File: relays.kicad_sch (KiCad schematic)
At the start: 0 parts

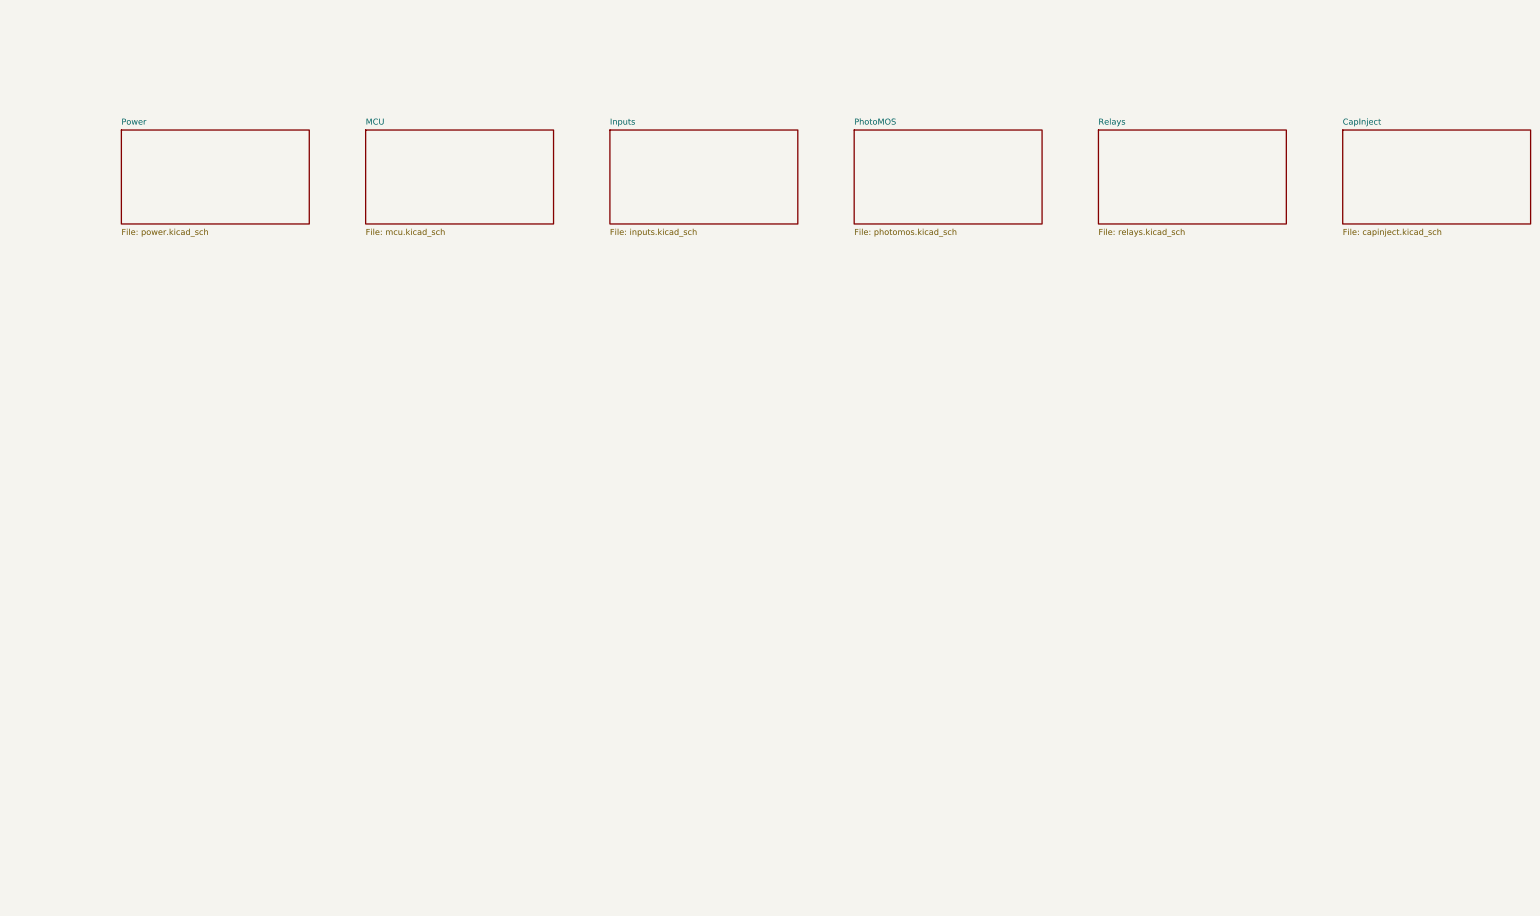
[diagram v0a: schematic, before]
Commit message: Realize ERC-clean KiCad schematic (rev 0.2)
Turn the paper design into a real KiCad 10 hierarchical schematic with
library symbols and footprints. 6 sheets: power, MCU, and full channel
counts (8 inputs, 8 PhotoMOS, 2 relays, 4 cap-inject) = 160 components.

- Replace AMS1117 with SY8089 buck (2.7-5.5Vin) for Wi-Fi-peak headroom.
- Input front-end uses 2.2k/1206 + EL357N (CRD dropped; poor LCSC stock).
- Verify key parts against JLCPCB (ESP32-S3 C2913198, SY8089 C78988,
  AQY212GS C719745, HK4100F C12072, USB-C C165948, AO3400A C20917).
- ERC passes 0 errors / 0 warnings; netlist verified, isolation barrier
  confirmed intact. No PCB layout yet (per request).
- Add Python generator (gen/) that emits the project and custom symbols.

Co-Authored-By: Claude Opus 4.7 <noreply@anthropic.com>
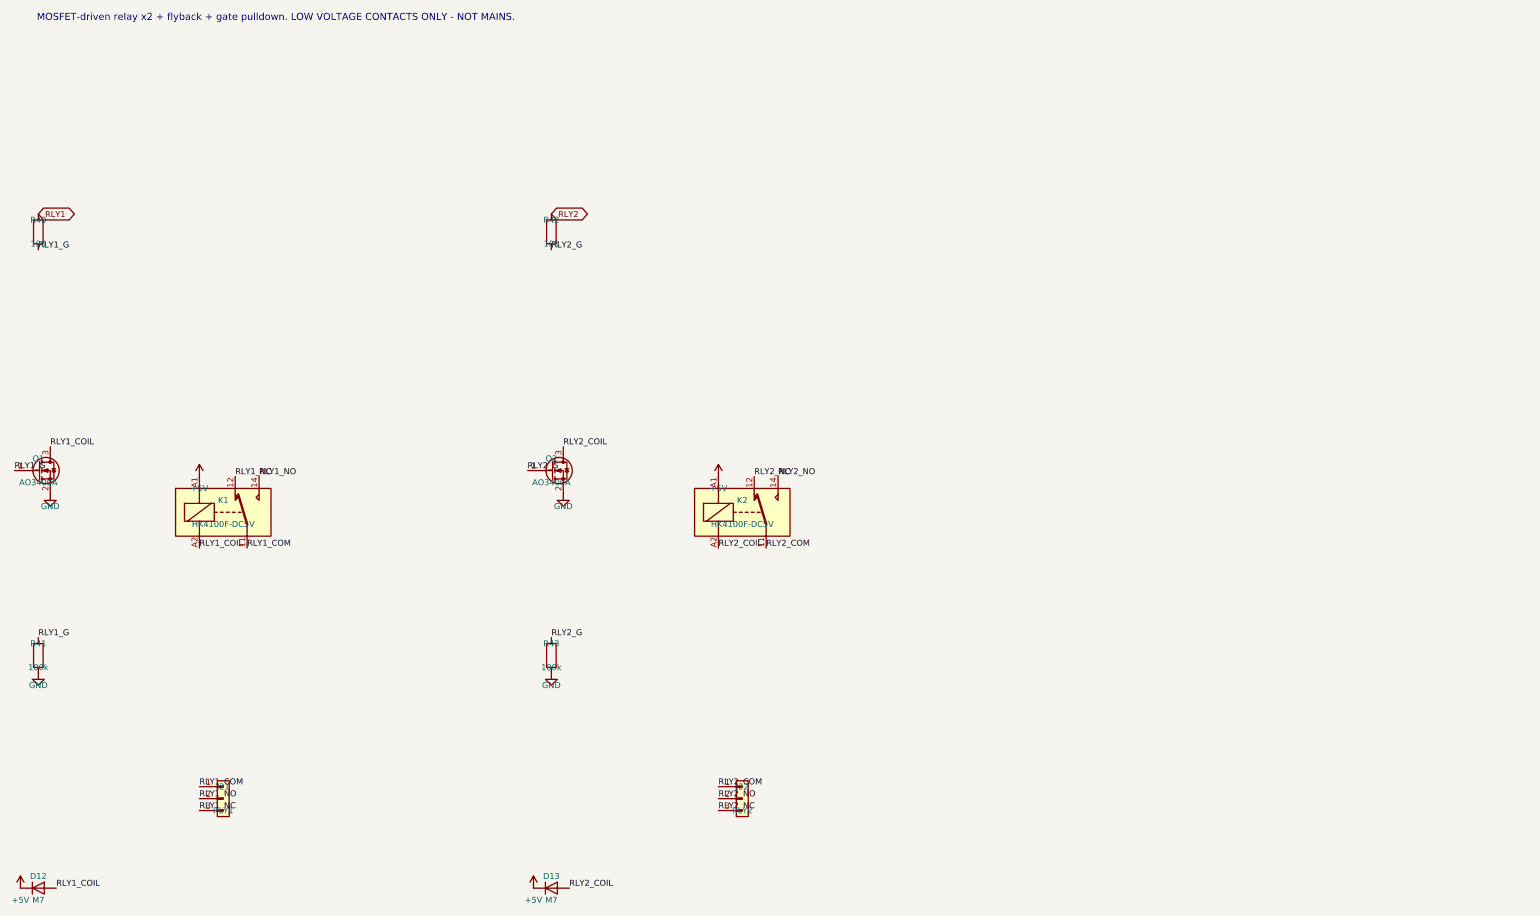
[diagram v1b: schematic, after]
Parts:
- added D12, D13: M7, Diode_SMD:D_SMA, symbol Device:D
- added J21: RLY1, TerminalBlock:TerminalBlock_MaiXu_MX126-5.0-03P_1x03_P5.00mm, symbol Connector_Generic:Conn_01x03
- added J22: RLY2, TerminalBlock:TerminalBlock_MaiXu_MX126-5.0-03P_1x03_P5.00mm, symbol Connector_Generic:Conn_01x03
- added K1, K2: HK4100F-DC5V, Relay_THT:Relay_SPDT_Fujitsu_FTR-LYCA005x_FormC_Vertical, symbol Relay:Relay_SPDT
- added Q1, Q2: AO3400A, Package_TO_SOT_SMD:SOT-23, symbol Transistor_FET:Q_NMOS_GSD
- added R40, R42: 100, Resistor_SMD:R_0603_1608Metric, symbol Device:R
- added R41, R43: 100k, Resistor_SMD:R_0603_1608Metric, symbol Device:R
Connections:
- new net +5V: D12.1 (K), D13.1 (K), K1.A1, K2.A1
- new net GND: Q1.2 (S), Q2.2 (S), R41.2, R43.2
- new net RLY1: R40.1
- new net RLY1_COIL: D12.2 (A), K1.A2, Q1.3 (D)
- new net RLY1_COM: J21.1 (Pin_1), K1.11
- new net RLY1_G: Q1.1 (G), R40.2, R41.1
- new net RLY1_NC: J21.3 (Pin_3), K1.12
- new net RLY1_NO: J21.2 (Pin_2), K1.14
- new net RLY2: R42.1
- new net RLY2_COIL: D13.2 (A), K2.A2, Q2.3 (D)
- new net RLY2_COM: J22.1 (Pin_1), K2.11
- new net RLY2_G: Q2.1 (G), R42.2, R43.1
- new net RLY2_NC: J22.3 (Pin_3), K2.12
- new net RLY2_NO: J22.2 (Pin_2), K2.14
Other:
- removed sheet CapInject
- removed sheet Inputs
- removed sheet MCU
- removed sheet PhotoMOS
- removed sheet Power
- removed sheet Relays
- note added: "MOSFET-driven relay x2 + flyback + gate pulldown. LOW VOLTAGE CONTACTS ONLY - NOT MAINS."
- title: Universal ESP32 Button/Signal Bridge -> 2x relay outputs  LV CONTACTS ONLY

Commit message: Add real footprints (HK4100F/AQY212GS/EL357N) + tidy schematic (rev 0.3)
- Build datasheet-accurate HK4100F-DC5V-SHG footprint (6-pad THT) and a
  matching symbol; coil=3/4, COM=5/6, NO=1, NC=2.
- Correct AQY212GS footprint to SOP-4 2.54mm pitch (was wrongly 1.27mm).
- Fix EL357N LCSC code C124981->C6649 (C124981 was a trimmer pot); add
  generated SOP-4 footprint.
- footprints/bridge.pretty generated from LCSC parts via easyeda2kicad.
- Re-lay-out all sheets for human review: labels offset from pins via
  short stubs routed by each pin's true orientation; 8-channel sheets on
  larger pages; clean per-channel columns.
- ERC still 0 errors / 0 warnings. Regenerated schematic.pdf, BOM, DESIGN.
- No PCB layout yet (paused per request).

Co-Authored-By: Claude Opus 4.7 <noreply@anthropic.com>
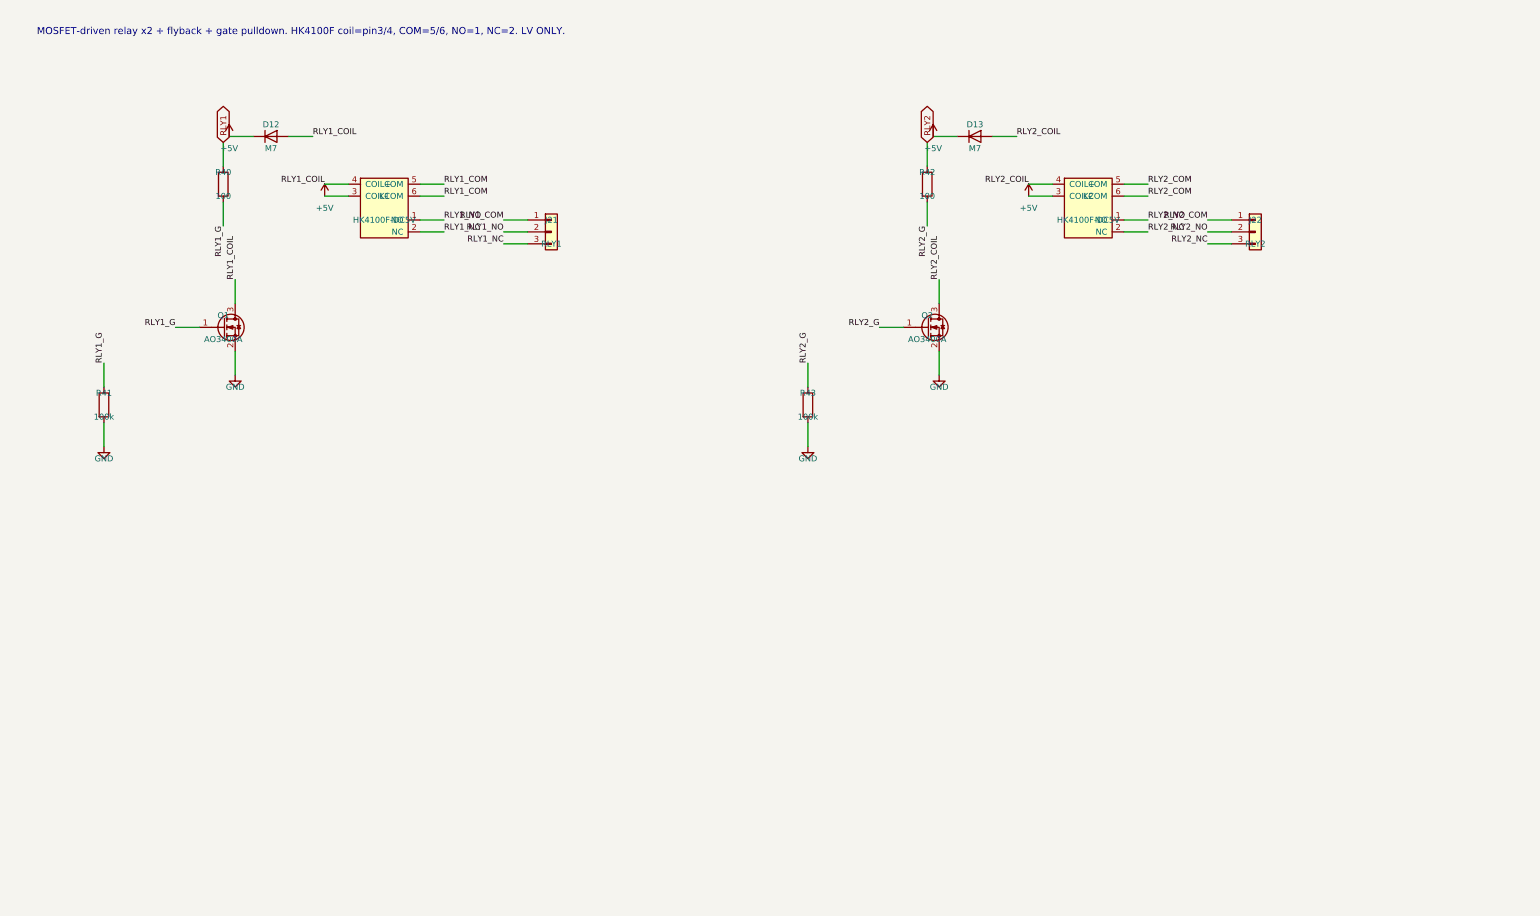
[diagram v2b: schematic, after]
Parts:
- removed K1, K2: HK4100F-DC5V, Relay_THT:Relay_SPDT_Fujitsu_FTR-LYCA005x_FormC_Vertical, symbol Relay:Relay_SPDT
- added K1, K2: HK4100F-DC5V, bridge:HK4100F-DC5V-SHG, symbol bridge:HK4100F
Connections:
- net +5V: now also K1.3 (COIL-), K2.3 (COIL-)
- net RLY1_COIL: now also K1.4 (COIL+)
- net RLY1_COM: now also K1.5 (COM), K1.6 (COM)
- net RLY1_NC: now also K1.2 (NC)
- net RLY1_NO: now also K1.1 (NO)
- net RLY2_COIL: now also K2.4 (COIL+)
- net RLY2_COM: now also K2.5 (COM), K2.6 (COM)
- net RLY2_NC: now also K2.2 (NC)
- net RLY2_NO: now also K2.1 (NO)
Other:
- note added: "MOSFET-driven relay x2 + flyback + gate pulldown. HK4100F coil=pin3/4, COM=5/6, NO=1, NC=2. LV ONLY."
- note removed: "MOSFET-driven relay x2 + flyback + gate pulldown. LOW VOLTAGE CONTACTS ONLY - NOT MAINS."
